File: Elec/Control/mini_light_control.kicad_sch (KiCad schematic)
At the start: 40 parts, among them J1 Conn_01x04, J2 Conn_01x02, J3 Conn_01x02, J4 Conn_01x03, J5 Conn_01x03, J6 Conn_01x02, J7 Conn_01x02, J8 Conn_01x03, J9 Conn_01x03, U1 LM2904DT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

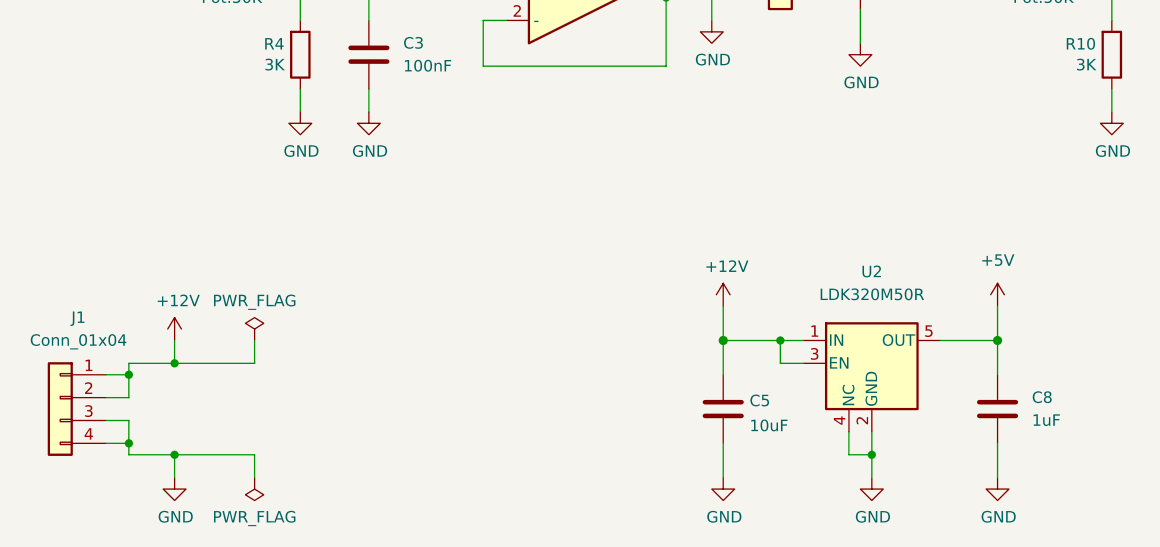
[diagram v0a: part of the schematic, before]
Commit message: Add protection diode for LDO and change power connector.
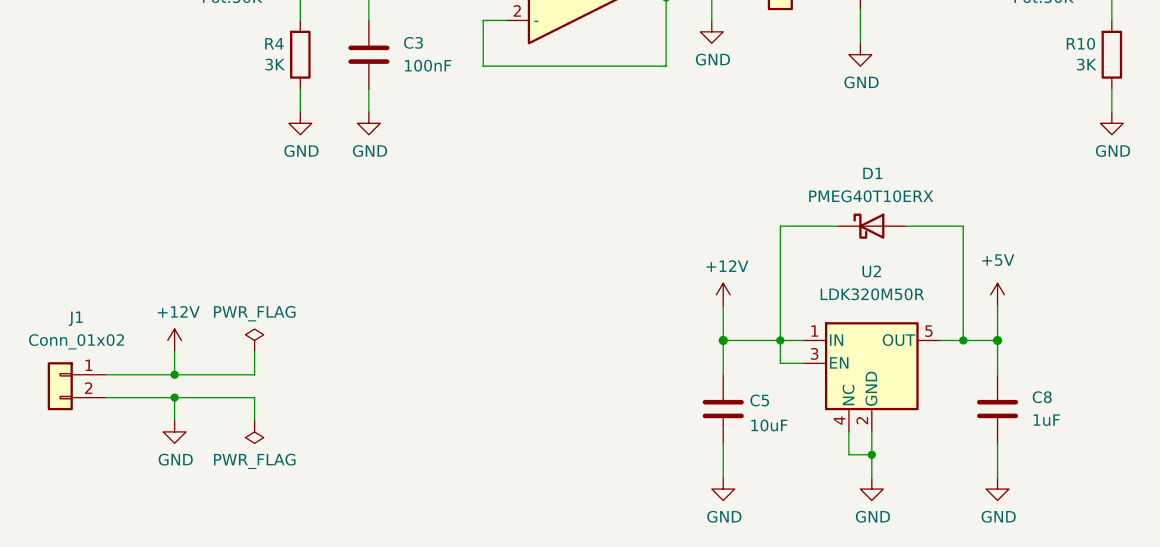
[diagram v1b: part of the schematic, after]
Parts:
- removed J1: Conn_01x04, Connector_JST:JST_PH_B4B-PH-K_1x04_P2.00mm_Vertical, symbol Connector_Generic:Conn_01x04
- added D1: PMEG40T10ERX, Diode_SMD:Nexperia_CFP3_SOD-123W, symbol Device:D_Schottky
- added J1: Conn_01x02, Connector_JST:JST_PH_B2B-PH-K_1x02_P2.00mm_Vertical, symbol Connector_Generic:Conn_01x02
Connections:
- net +12V: now also D1.1 (K), J1.1 (Pin_1)
- net +5V: now also D1.2 (A)
- net GND: now also J1.2 (Pin_2)

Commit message: Change simbol connector to 'MountingPin' version
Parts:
- J4, J5, J8, J9: symbol Connector_Generic:Conn_01x03 -> Connector_Generic_MountingPin:Conn_01x03_MountingPin
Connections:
- net GND: now also J4.MP (MountPin), J5.MP (MountPin), J8.MP (MountPin), J9.MP (MountPin)
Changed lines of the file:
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@@
   (junction (at 110.49 78.74) (diameter 0) (color 0 0 0 0))
   (junction (at 110.49 127) (diameter 0) (color 0 0 0 0))
+  (junction (at 115.57 86.36) (diameter 0) (color 0 0 0 0))
+  (junction (at 115.57 134.62) (diameter 0) (color 0 0 0 0))
   (junction (at 116.84 165.1) (diameter 1.016) (color 0 0 0 0))
   (junction (at 123.19 165.1) (diameter 0) (color 0 0 0 0))
@@
   (junction (at 200.66 78.74) (diameter 0) (color 0 0 0 0))
   (junction (at 200.66 127) (diameter 0) (color 0 0 0 0))
+  (junction (at 205.74 86.36) (diameter 0) (color 0 0 0 0))
+  (junction (at 205.74 134.62) (diameter 0) (color 0 0 0 0))
   (wire (pts (xy 48.26 168.91) (xy 55.88 168.91))
     (stroke (width 0) (type solid) (color 0 0 0 0))
@@
     (stroke (width 0) (type default) (color 0 0 0 0))
   )
-  (wire (pts (xy 115.57 76.2) (xy 115.57 81.28))
+  (wire (pts (xy 115.57 76.2) (xy 115.57 86.36))
+    (stroke (width 0) (type default) (color 0 0 0 0))
+  )
+  (wire (pts (xy 115.57 86.36) (xy 115.57 87.63))
     (stroke (width 0) (type default) (color 0 0 0 0))
   )
@@
     (stroke (width 0) (type default) (color 0 0 0 0))
   )
-  (wire (pts (xy 115.57 124.46) (xy 115.57 129.54))
+  (wire (pts (xy 115.57 124.46) (xy 115.57 134.62))
+    (stroke (width 0) (type default) (color 0 0 0 0))
+  )
+  (wire (pts (xy 115.57 134.62) (xy 115.57 135.89))
     (stroke (width 0) (type default) (color 0 0 0 0))
   )
@@
     (stroke (width 0) (type default) (color 0 0 0 0))
   )
+  (wire (pts (xy 123.19 83.82) (xy 123.19 86.36))
+    (stroke (width 0) (type default) (color 0 0 0 0))
+  )
+  (wire (pts (xy 123.19 86.36) (xy 115.57 86.36))
+    (stroke (width 0) (type default) (color 0 0 0 0))
+  )
+  (wire (pts (xy 123.19 132.08) (xy 123.19 134.62))
+    (stroke (width 0) (type default) (color 0 0 0 0))
+  )
+  (wire (pts (xy 123.19 134.62) (xy 115.57 134.62))
+    (stroke (width 0) (type default) (color 0 0 0 0))
+  )
   (wire (pts (xy 123.19 152.4) (xy 123.19 165.1))
     (stroke (width 0) (type default) (color 0 0 0 0))
@@
     (stroke (width 0) (type default) (color 0 0 0 0))
   )
-  (wire (pts (xy 205.74 76.2) (xy 205.74 81.28))
+  (wire (pts (xy 205.74 76.2) (xy 205.74 86.36))
+    (stroke (width 0) (type default) (color 0 0 0 0))
+  )
+  (wire (pts (xy 205.74 86.36) (xy 205.74 87.63))
     (stroke (width 0) (type default) (color 0 0 0 0))
   )
@@
     (stroke (width 0) (type default) (color 0 0 0 0))
   )
-  (wire (pts (xy 205.74 124.46) (xy 205.74 129.54))
+  (wire (pts (xy 205.74 124.46) (xy 205.74 134.62))
+    (stroke (width 0) (type default) (color 0 0 0 0))
+  )
+  (wire (pts (xy 205.74 134.62) (xy 205.74 135.89))
     (stroke (width 0) (type default) (color 0 0 0 0))
   )
@@
   )
   (wire (pts (xy 208.28 124.46) (xy 205.74 124.46))
+    (stroke (width 0) (type default) (color 0 0 0 0))
+  )
+  (wire (pts (xy 213.36 83.82) (xy 213.36 86.36))
+    (stroke (width 0) (type default) (color 0 0 0 0))
+  )
+  (wire (pts (xy 213.36 86.36) (xy 205.74 86.36))
+    (stroke (width 0) (type default) (color 0 0 0 0))
+  )
+  (wire (pts (xy 213.36 132.08) (xy 213.36 134.62))
+    (stroke (width 0) (type default) (color 0 0 0 0))
+  )
+  (wire (pts (xy 213.36 134.62) (xy 205.74 134.62))
     (stroke (width 0) (type default) (color 0 0 0 0))
   )
@@
     (pin "1")
   )
-  (symbol (lib_id "power:GND") (at 115.57 81.28 0) (unit 1)
-    (in_bom yes) (on_board yes)
-    (property "Reference" "#PWR014" (id 0) (at 115.57 87.63 0)
-      (effects (font (size 1.27 1.27)) hide)
-    )
-    (property "Value" "GND" (id 1) (at 115.697 85.6742 0))
-    (property "Footprint" "" (id 2) (at 115.57 81.28 0)
-      (effects (font (size 1.27 1.27)) hide)
-    )
-    (property "Datasheet" "" (id 3) (at 115.57 81.28 0)
-      (effects (font (size 1.27 1.27)) hide)
-    )
-    (pin "1")
-  )
-  (symbol (lib_id "power:GND") (at 115.57 129.54 0) (unit 1)
-    (in_bom yes) (on_board yes)
-    (property "Reference" "#PWR016" (id 0) (at 115.57 135.89 0)
-      (effects (font (size 1.27 1.27)) hide)
-    )
-    (property "Value" "GND" (id 1) (at 115.697 133.9342 0))
-    (property "Footprint" "" (id 2) (at 115.57 129.54 0)
-      (effects (font (size 1.27 1.27)) hide)
-    )
-    (property "Datasheet" "" (id 3) (at 115.57 129.54 0)
+  (symbol (lib_id "power:GND") (at 115.57 87.63 0) (unit 1)
+    (in_bom yes) (on_board yes)
+    (property "Reference" "#PWR014" (id 0) (at 115.57 93.98 0)
+      (effects (font (size 1.27 1.27)) hide)
+    )
+    (property "Value" "GND" (id 1) (at 115.697 92.0242 0))
+    (property "Footprint" "" (id 2) (at 115.57 87.63 0)
+      (effects (font (size 1.27 1.27)) hide)
+    )
+    (property "Datasheet" "" (id 3) (at 115.57 87.63 0)
+      (effects (font (size 1.27 1.27)) hide)
+    )
+    (pin "1")
+  )
+  (symbol (lib_id "power:GND") (at 115.57 135.89 0) (unit 1)
+    (in_bom yes) (on_board yes)
+    (property "Reference" "#PWR016" (id 0) (at 115.57 142.24 0)
+      (effects (font (size 1.27 1.27)) hide)
+    )
+    (property "Value" "GND" (id 1) (at 115.697 140.2842 0))
+    (property "Footprint" "" (id 2) (at 115.57 135.89 0)
+      (effects (font (size 1.27 1.27)) hide)
+    )
+    (property "Datasheet" "" (id 3) (at 115.57 135.89 0)
       (effects (font (size 1.27 1.27)) hide)
     )
@@
     (pin "1")
   )
-  (symbol (lib_id "power:GND") (at 205.74 81.28 0) (unit 1)
-    (in_bom yes) (on_board yes)
-    (property "Reference" "#PWR037" (id 0) (at 205.74 87.63 0)
-      (effects (font (size 1.27 1.27)) hide)
-    )
-    (property "Value" "GND" (id 1) (at 205.867 85.6742 0))
-    (property "Footprint" "" (id 2) (at 205.74 81.28 0)
-      (effects (font (size 1.27 1.27)) hide)
-    )
-    (property "Datasheet" "" (id 3) (at 205.74 81.28 0)
-      (effects (font (size 1.27 1.27)) hide)
-    )
-    (pin "1")
-  )
-  (symbol (lib_id "power:GND") (at 205.74 129.54 0) (unit 1)
-    (in_bom yes) (on_board yes)
-    (property "Reference" "#PWR039" (id 0) (at 205.74 135.89 0)
-      (effects (font (size 1.27 1.27)) hide)
-    )
-    (property "Value" "GND" (id 1) (at 205.867 133.9342 0))
-    (property "Footprint" "" (id 2) (at 205.74 129.54 0)
-      (effects (font (size 1.27 1.27)) hide)
-    )
-    (property "Datasheet" "" (id 3) (at 205.74 129.54 0)
+  (symbol (lib_id "power:GND") (at 205.74 87.63 0) (unit 1)
+    (in_bom yes) (on_board yes)
+    (property "Reference" "#PWR037" (id 0) (at 205.74 93.98 0)
+      (effects (font (size 1.27 1.27)) hide)
+    )
+    (property "Value" "GND" (id 1) (at 205.867 92.0242 0))
+    (property "Footprint" "" (id 2) (at 205.74 87.63 0)
+      (effects (font (size 1.27 1.27)) hide)
+    )
+    (property "Datasheet" "" (id 3) (at 205.74 87.63 0)
+      (effects (font (size 1.27 1.27)) hide)
+    )
+    (pin "1")
+  )
+  (symbol (lib_id "power:GND") (at 205.74 135.89 0) (unit 1)
+    (in_bom yes) (on_board yes)
+    (property "Reference" "#PWR039" (id 0) (at 205.74 142.24 0)
+      (effects (font (size 1.27 1.27)) hide)
+    )
+    (property "Value" "GND" (id 1) (at 205.867 140.2842 0))
+    (property "Footprint" "" (id 2) (at 205.74 135.89 0)
+      (effects (font (size 1.27 1.27)) hide)
+    )
+    (property "Datasheet" "" (id 3) (at 205.74 135.89 0)
       (effects (font (size 1.27 1.27)) hide)
     )
@@
     (pin "2")
   )
-  (symbol (lib_id "Connector_Generic:Conn_01x03") (at 123.19 76.2 0) (unit 1)
+  (symbol (lib_id "Connector_Generic_MountingPin:Conn_01x03_MountingPin") (at 123.19 76.2 0) (unit 1)
     (in_bom yes) (on_board yes)
     (property "Reference" "J4" (id 0) (at 125.222 75.1332 0)
@@
     (pin "2")
     (pin "3")
-  )
-  (symbol (lib_id "Connector_Generic:Conn_01x03") (at 123.19 124.46 0) (unit 1)
+    (pin "MP")
+  )
+  (symbol (lib_id "Connector_Generic_MountingPin:Conn_01x03_MountingPin") (at 123.19 124.46 0) (unit 1)
     (in_bom yes) (on_board yes)
     (property "Reference" "J5" (id 0) (at 125.222 123.3932 0)
@@
       (effects (font (size 1.27 1.27)) hide)
     )
-    (property "Datasheet" "https://www.jst.fr/core/file.get?path=doc/jst/family/pdf/ePH.pdf" (id 3) (at 123.19 124.46 0)
+    (property "Datasheet" "~" (id 3) (at 123.19 124.46 0)
       (effects (font (size 1.27 1.27)) hide)
     )
@@
     (pin "2")
     (pin "3")
-  )
-  (symbol (lib_id "Connector_Generic:Conn_01x03") (at 213.36 76.2 0) (unit 1)
+    (pin "MP")
+  )
+  (symbol (lib_id "Connector_Generic_MountingPin:Conn_01x03_MountingPin") (at 213.36 76.2 0) (unit 1)
     (in_bom yes) (on_board yes)
     (property "Reference" "J8" (id 0) (at 215.392 75.1332 0)
@@
       (effects (font (size 1.27 1.27)) hide)
     )
-    (property "Datasheet" "https://www.jst.fr/core/file.get?path=doc/jst/family/pdf/ePH.pdf" (id 3) (at 213.36 76.2 0)
+    (property "Datasheet" "~" (id 3) (at 213.36 76.2 0)
       (effects (font (size 1.27 1.27)) hide)
     )
@@
     (pin "2")
     (pin "3")
-  )
-  (symbol (lib_id "Connector_Generic:Conn_01x03") (at 213.36 124.46 0) (unit 1)
+    (pin "MP")
+  )
+  (symbol (lib_id "Connector_Generic_MountingPin:Conn_01x03_MountingPin") (at 213.36 124.46 0) (unit 1)
     (in_bom yes) (on_board yes)
     (property "Reference" "J9" (id 0) (at 215.392 123.3932 0)
@@
       (effects (font (size 1.27 1.27)) hide)
     )
-    (property "Datasheet" "https://www.jst.fr/core/file.get?path=doc/jst/family/pdf/ePH.pdf" (id 3) (at 213.36 124.46 0)
+    (property "Datasheet" "~" (id 3) (at 213.36 124.46 0)
       (effects (font (size 1.27 1.27)) hide)
     )
@@
     (pin "2")
     (pin "3")
+    (pin "MP")
   )
   (symbol (lib_id "Device:Opamp_Dual") (at 100.33 78.74 0) (unit 2)

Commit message: Change JST connector polarity + regenerate gerber file
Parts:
- U2: symbol antoine163:LDK320M50R -> AM163:LDK320M50R
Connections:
- net at C3.1, R4.2, R6.1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: now also J3.2 (Pin_2); no longer J3.1 (Pin_1)
- net at C9.1, R11.1, R8.2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: now also J6.2 (Pin_2); no longer J6.1 (Pin_1)
- net at C10.1, R10.2, R12.1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: now also J7.2 (Pin_2); no longer J7.1 (Pin_1)
- net at R9.1: now also J7.1 (Pin_1); no longer J7.2 (Pin_2)
- net at R7.1: now also J6.1 (Pin_1); no longer J6.2 (Pin_2)
- net at C2.1, R2.2, R5.1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: now also J2.2 (Pin_2); no longer J2.1 (Pin_1)
- net at R1.1: now also J2.1 (Pin_1); no longer J2.2 (Pin_2)
- net at R3.1: now also J3.1 (Pin_1); no longer J3.2 (Pin_2)
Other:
- moved on the sheet: J2, J3, J6, J7
